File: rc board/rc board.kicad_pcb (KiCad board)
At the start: 2 copper layers, 12 parts, among them U1 DRV10983

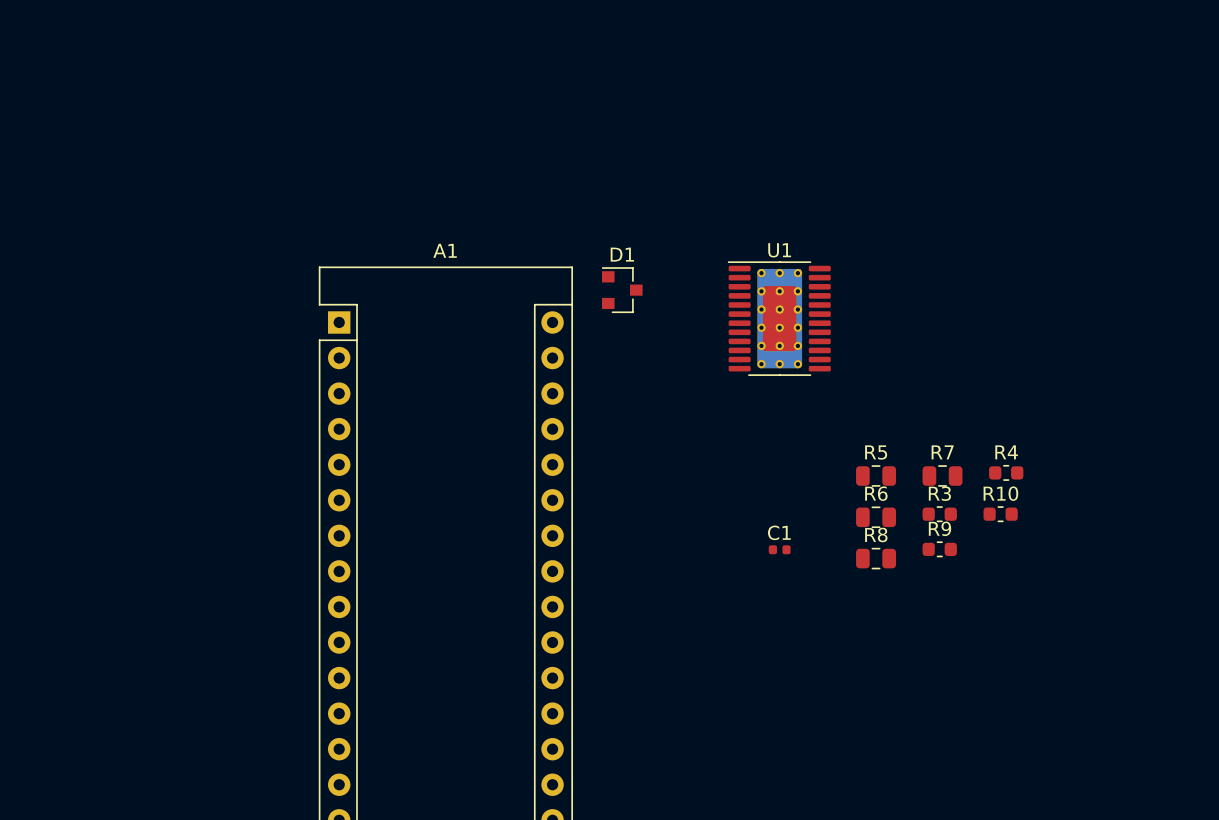
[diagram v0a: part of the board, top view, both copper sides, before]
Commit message: Finiched the driver part, and assigned the IOs to the uC.
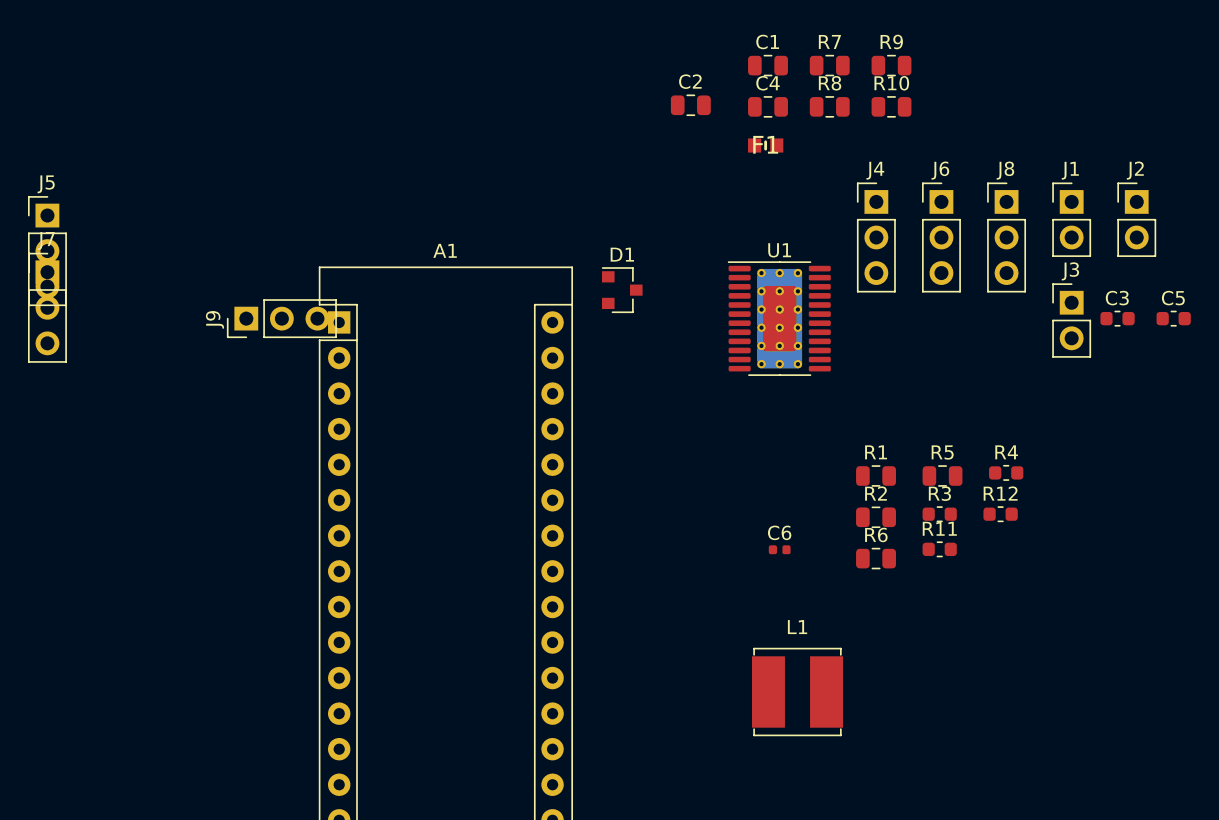
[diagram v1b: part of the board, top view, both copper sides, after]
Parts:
- added C1: 10uF, Capacitor_SMD:C_0805_2012Metric, F.Cu at (104.6, 11.1)
- added C2: 10uF, Capacitor_SMD:C_0805_2012Metric, F.Cu at (99.1, 14.0)
- added C3: 0.1uF, Capacitor_SMD:C_0603_1608Metric, F.Cu at (129.5, 29.2)
- added C4: 10uF, Capacitor_SMD:C_0805_2012Metric, F.Cu at (104.6, 14.1)
- added C5: 1uF, Capacitor_SMD:C_0603_1608Metric, F.Cu at (133.6, 29.2)
- added F1: 370mA, Fuse:FUSC1607X85N, F.Cu at (104.4, 16.8)
- added J1: Throttle_bypass, Connector_PinHeader_2.54mm:PinHeader_1x02_P2.54mm_Vertical, F.Cu at (126.3, 20.9)
- added J2: CH3_bypass, Connector_PinHeader_2.54mm:PinHeader_1x02_P2.54mm_Vertical, F.Cu at (130.9, 20.9)
- added J3: Steering_bypass, Connector_PinHeader_2.54mm:PinHeader_1x02_P2.54mm_Vertical, F.Cu at (126.3, 28.1)
- added J4: Throttle_in, Connector_PinHeader_2.54mm:PinHeader_1x03_P2.54mm_Vertical, F.Cu at (112.3, 20.9)
- added J5: Throttle_out, Connector_PinHeader_2.54mm:PinHeader_1x03_P2.54mm_Vertical, F.Cu at (53.1, 21.8)
- added J6: CH3_in, Connector_PinHeader_2.54mm:PinHeader_1x03_P2.54mm_Vertical, F.Cu at (117.0, 20.9)
- added J7: CH3_out, Connector_PinHeader_2.54mm:PinHeader_1x03_P2.54mm_Vertical, F.Cu at (53.1, 25.9)
- added J8: Steering_in, Connector_PinHeader_2.54mm:PinHeader_1x03_P2.54mm_Vertical, F.Cu at (121.6, 20.9)
- added J9: Steering_out, Connector_PinHeader_2.54mm:PinHeader_1x03_P2.54mm_Vertical, F.Cu at (67.3, 29.2)
- added L1: L_Core_Ferrite_Small, Inductor_SMD:L_Bourns_SRN6045TA, F.Cu at (106.7, 55.9)
- added R10: 10, Resistor_SMD:R_0805_2012Metric, F.Cu at (113.4, 14.1)
- added R7: 10, Resistor_SMD:R_0805_2012Metric, F.Cu at (109.0, 11.1)
- added R8: 10, Resistor_SMD:R_0805_2012Metric, F.Cu at (109.0, 14.1)
- added R9: 10, Resistor_SMD:R_0805_2012Metric, F.Cu at (113.4, 11.1)
- renumbered C1 to C6, R5 to R1, R9 to R11, R10 to R12, R6 to R2, R7 to R5, R8 to R6
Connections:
- C6 pad 1: Net-(C1-Pad1) -> Net-(C6-Pad1)
- C6 pad 2: Net-(C1-Pad2) -> Net-(C6-Pad2)
- U1 pad 1: (no net) -> Net-(C3-Pad2)
- U1 pad 17: Net-(U1-Pad17) -> U_0
- U1 pad 18: Net-(U1-Pad18) -> U_0
- U1 pad 19: Net-(U1-Pad19) -> V_0
- U1 pad 2: Net-(U1-Pad2) -> Net-(C6-Pad1)
- U1 pad 20: Net-(U1-Pad20) -> V_0
- U1 pad 21: Net-(U1-Pad21) -> W_0
- U1 pad 22: Net-(U1-Pad22) -> W_0
- U1 pad 3: Net-(U1-Pad3) -> Net-(C6-Pad2)
- U1 pad 6: Net-(U1-Pad6) -> +5V_0

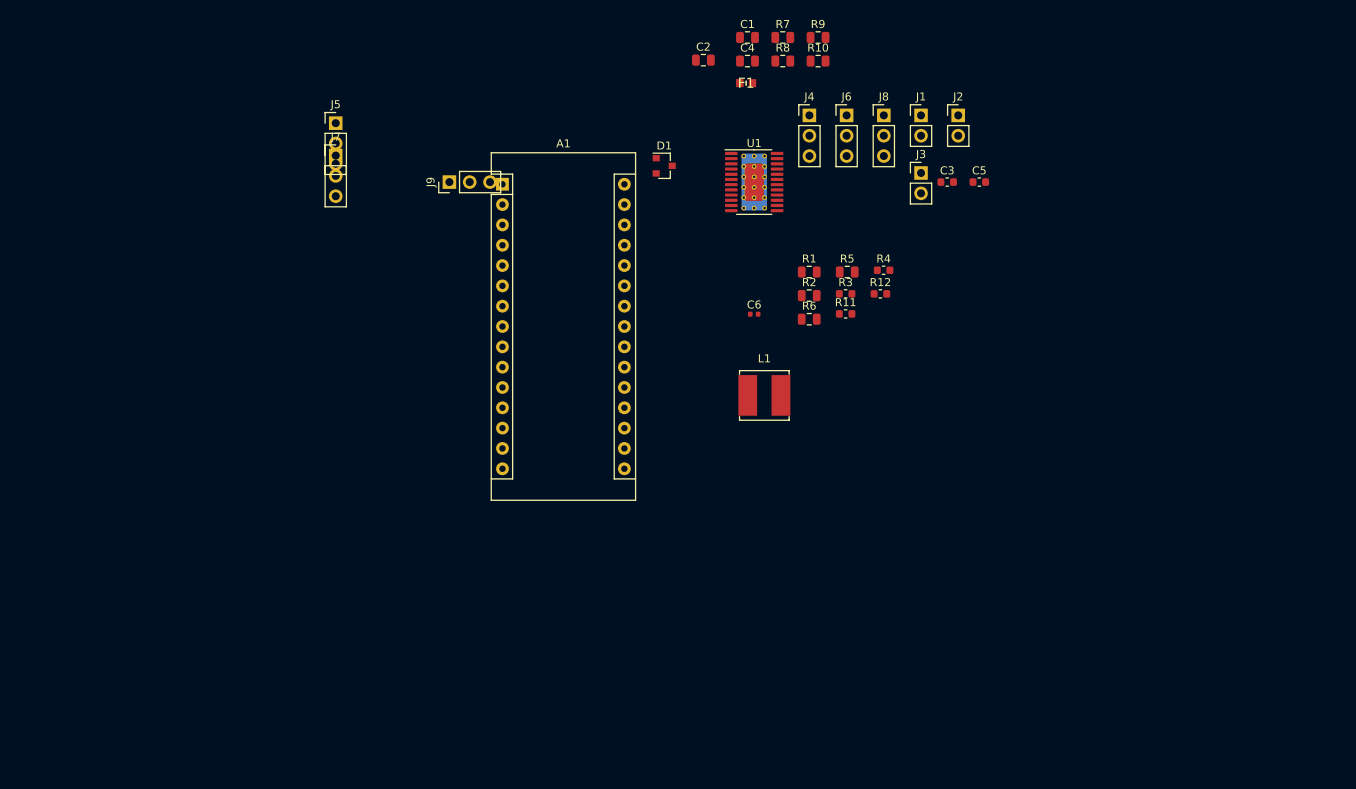
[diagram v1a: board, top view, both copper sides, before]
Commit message: Added schottkyes for automatic battery compatibility, and started component layout.
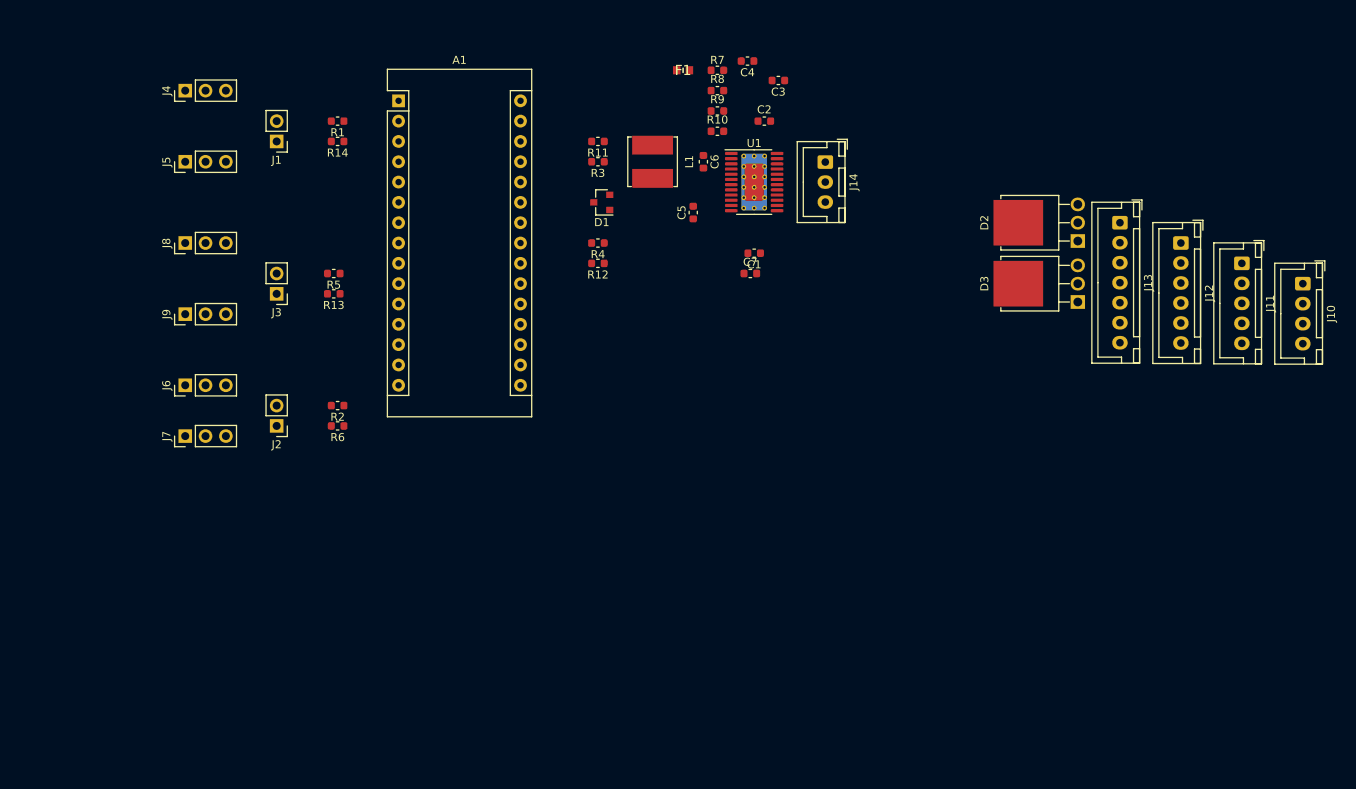
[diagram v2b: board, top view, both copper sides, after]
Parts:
- added C7: 10uF, Capacitor_SMD:C_0603_1608Metric, F.Cu at (104.9, 40.6)
- added D2: MBR2045CTI, Package_TO_SOT_THT:TO-251-3-1EP_Horizontal_TabDown, F.Cu at (145.9, 36.6)
- added D3: MBR2045CTI, Package_TO_SOT_THT:TO-251-3-1EP_Horizontal_TabDown, F.Cu at (145.9, 44.2)
- added J10: 3S, Connector_JST:JST_XH_B4B-XH-A_1x04_P2.50mm_Vertical, F.Cu at (174.0, 41.9)
- added J11: 4S, Connector_JST:JST_XH_B5B-XH-A_1x05_P2.50mm_Vertical, F.Cu at (166.4, 39.4)
- added J12: 5S, Connector_JST:JST_XH_B6B-XH-A_1x06_P2.50mm_Vertical, F.Cu at (158.8, 36.8)
- added J13: 6S, Connector_JST:JST_XH_B7B-XH-A_1x07_P2.50mm_Vertical, F.Cu at (151.1, 34.3)
- added J14: Mot_0, Connector_JST:JST_XH_B3B-XH-A_1x03_P2.50mm_Vertical, F.Cu at (114.3, 26.7)
- added R13: 10k, Resistor_SMD:R_0603_1608Metric, F.Cu at (52.9, 43.2)
- added R14: 10k, Resistor_SMD:R_0603_1608Metric, F.Cu at (53.3, 24.1)
- C1: value 10uF -> 1uF; footprint Capacitor_SMD:C_0805_2012Metric -> Capacitor_SMD:C_0603_1608Metric
- C2, C4: footprint Capacitor_SMD:C_0805_2012Metric -> Capacitor_SMD:C_0603_1608Metric
- C3: value 0.1uF -> 100nF
- C6: value 0.01nF -> 10nF; footprint Capacitor_SMD:C_0402_1005Metric -> Capacitor_SMD:C_0603_1608Metric
- J1: value Throttle_bypass -> Bypass
- J2: value CH3_bypass -> Bypass
- J3: value Steering_bypass -> Bypass
- L1: value L_Core_Ferrite_Small -> 47 uH
- R1, R2, R5, R6: value 10 -> 10k; footprint Resistor_SMD:R_0805_2012Metric -> Resistor_SMD:R_0603_1608Metric
- R10, R7, R8, R9: footprint Resistor_SMD:R_0805_2012Metric -> Resistor_SMD:R_0603_1608Metric
- moved J2 93.6 mm to (45.7, 59.7), turned to 180 degrees
- moved J6 89.3 mm to (34.3, 54.6), turned to 90 degrees
- moved J8 88.8 mm to (34.3, 36.8), turned to 90 degrees
- moved J3 81.9 mm to (45.7, 43.2), turned to 180 degrees
- moved J1 80.6 mm to (45.7, 24.1), turned to 180 degrees
- moved J4 78.1 mm to (34.3, 17.8), turned to 90 degrees
- moved R5 64.2 mm to (52.9, 40.6), turned to 180 degrees
- moved R1 61.9 mm to (53.3, 21.6), turned to 180 degrees
- moved R2 60.5 mm to (53.3, 57.1), turned to 180 degrees
- moved R6 60.4 mm to (53.3, 59.7), turned to 180 degrees
- moved J7 39.8 mm to (34.3, 61.0), turned to 90 degrees
- moved R11 37.7 mm to (85.9, 24.1), turned to 180 degrees
- moved J9 36.9 mm to (34.3, 45.7)
- moved C5 36.0 mm to (97.8, 33.0), turned to 90 degrees
- moved R4 35.9 mm to (85.9, 36.8), turned to 180 degrees
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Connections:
- net Net-(A1-Pad10) renamed EN_3
- net Net-(A1-Pad7) renamed EN_1
- net Net-(A1-Pad9) renamed EN_2
- net Net-(J1-Pad1) renamed Throttle_in
- net Net-(J3-Pad1) renamed Steering_in
- A1 pad 11: Net-(A1-Pad11) -> DIR
- A1 pad 19: Net-(A1-Pad19) -> Batt_0
- A1 pad 20: Net-(A1-Pad20) -> Batt_1
- A1 pad 21: Net-(A1-Pad21) -> Batt_2
- A1 pad 22: Net-(A1-Pad22) -> Batt_3
- A1 pad 25: Net-(A1-Pad25) -> Batt_4
- A1 pad 26: Net-(A1-Pad26) -> Batt_5
- A1 pad 27: +3V3 -> +5V
- A1 pad 5: Net-(A1-Pad5) -> EN_0
- C1 pad 2: +3V3 -> Net-(C1-Pad2)
- J1 pad 2: Net-(J1-Pad2) -> Throttle_out
- J2 pad 1: Net-(J2-Pad1) -> CH3_in
- J2 pad 2: Net-(J2-Pad2) -> CH3_out
- J3 pad 2: Net-(J3-Pad2) -> Steering_out
- J4 pad 3: Net-(J1-Pad2) -> Throttle_out
- J6 pad 3: Net-(J2-Pad2) -> CH3_out
- J7 pad 3: Net-(J2-Pad1) -> CH3_in
- J8 pad 3: Net-(J3-Pad2) -> Steering_out
- R1 pad 1: +3V3 -> Net-(A1-Pad6)
- R1 pad 2: +3.3V_0 -> Throttle_out
- R2 pad 1: +3V3 -> Net-(A1-Pad8)
- R2 pad 2: +3.3V_1 -> CH3_out
- R3 pad 1: Net-(D1-Pad1) -> Net-(D1-Pad2)
- R4 pad 1: Net-(D1-Pad2) -> Net-(D1-Pad1)
- R5 pad 1: +3V3 -> Net-(A1-Pad12)
- R5 pad 2: +3.3V_2 -> Steering_out
- R6 pad 1: +3V3 -> Net-(A1-Pad13)
- R6 pad 2: +3.3V_3 -> CH3_in
- U1 pad 10: Net-(D1-Pad1) -> Net-(D1-Pad2)
- U1 pad 11: Net-(D1-Pad2) -> Net-(D1-Pad1)
- U1 pad 14: DIR_0 -> DIR
- U1 pad 9: +3.3V_0 -> Net-(C1-Pad2)

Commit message: More routing, added the second driver.
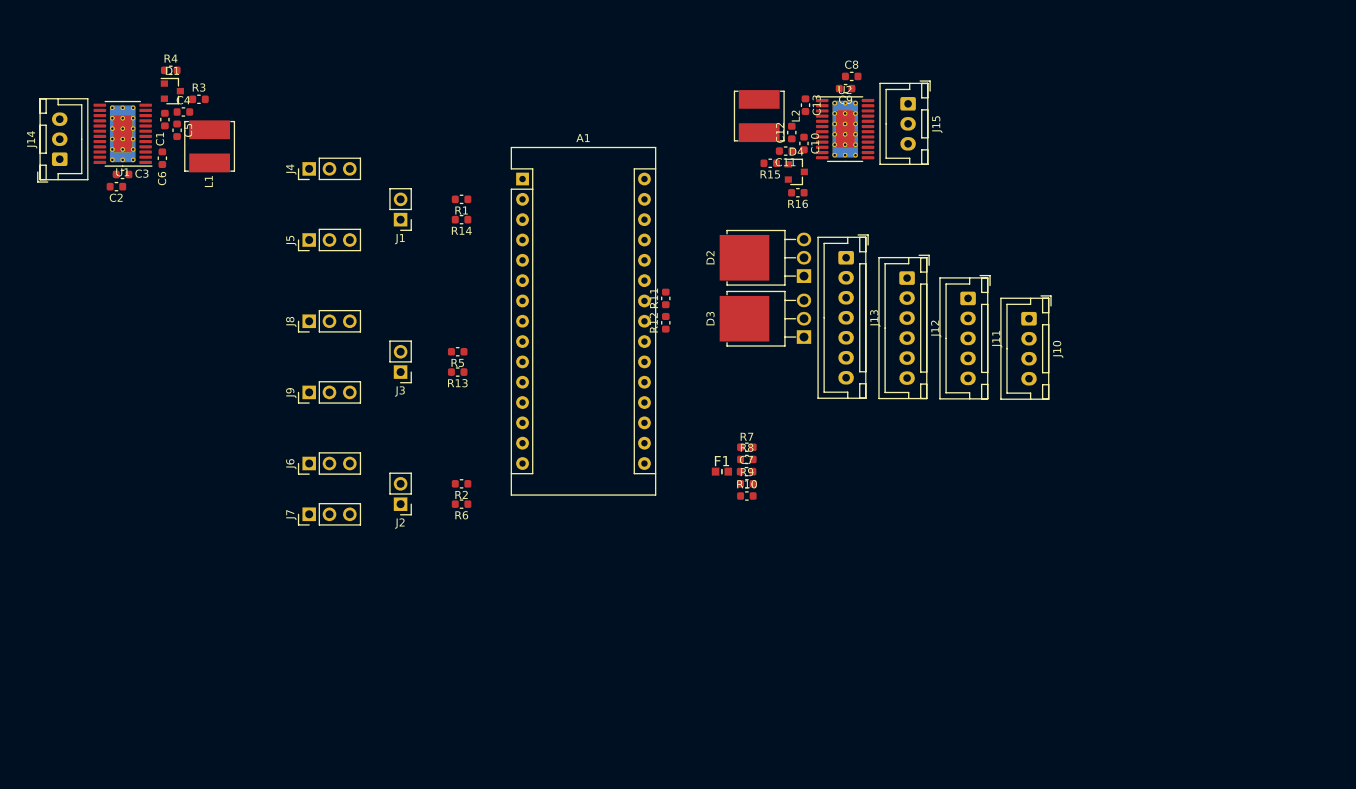
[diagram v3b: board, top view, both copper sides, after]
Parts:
- added C10: 1uF, Capacitor_SMD:C_0603_1608Metric, F.Cu at (111.6, 24.4)
- added C11: 10uF, Capacitor_SMD:C_0603_1608Metric, F.Cu at (109.3, 25.3)
- added C12: 1uF, Capacitor_SMD:C_0603_1608Metric, F.Cu at (110.1, 23.0)
- added C13: 10nF, Capacitor_SMD:C_0603_1608Metric, F.Cu at (111.8, 19.6)
- added C8: 10uF, Capacitor_SMD:C_0603_1608Metric, F.Cu at (117.6, 16.0)
- added C9: 100nF, Capacitor_SMD:C_0603_1608Metric, F.Cu at (116.8, 17.5)
- added D4: BAW56LT3G, Package_TO_SOT_SMD:SOT-23, F.Cu at (110.7, 27.9)
- added J15: Mot_0, Connector_JST:JST_XH_B3B-XH-A_1x03_P2.50mm_Vertical, F.Cu at (124.7, 19.4)
- added L2: 47 uH, Inductor_SMD:L_Bourns_SRN6045TA, F.Cu at (106.0, 21.0)
- added R15: 10k, Resistor_SMD:R_0603_1608Metric, F.Cu at (107.4, 26.9)
- added R16: 10k, Resistor_SMD:R_0603_1608Metric, F.Cu at (110.9, 30.5)
- added U2: DRV10983, Package_SO:HTSSOP-24-1EP_4.4x7.8mm_P0.65mm_EP3.4x7.8mm_Mask2.4x4.68mm_ThermalVias, F.Cu at (116.8, 22.6)
- moved J14 95.7 mm to (18.6, 26.4), turned to 90 degrees
- moved C3 82.8 mm to (26.5, 28.3), turned to 0 degrees
- moved C2 81.4 mm to (25.7, 29.8), turned to 180 degrees
- moved U1 79.2 mm to (26.5, 23.2), turned to 180 degrees
- moved C1 75.5 mm to (31.8, 21.4), turned to 90 degrees
- moved C4 70.8 mm to (34.1, 20.4), turned to 0 degrees
- moved C6 67.6 mm to (31.4, 26.2), turned to 90 degrees
- moved C5 65.3 mm to (33.3, 22.7), turned to 270 degrees
- moved R4 57.6 mm to (32.5, 15.2), turned to 0 degrees
- moved D1 55.4 mm to (32.7, 17.8), turned to 0 degrees
- moved L1 55.4 mm to (37.3, 24.7), turned to 90 degrees
- moved R3 50.5 mm to (36.0, 18.9), turned to 0 degrees
- moved F1 50.4 mm to (101.4, 65.4)
- moved R7 47.3 mm to (104.5, 62.4)
- moved R9 46.8 mm to (104.5, 66.9)
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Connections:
- A1 pad 17: Net-(A1-Pad17) -> +3V3
- A1 pad 19: Batt_0 -> Batt_0_sense
- A1 pad 20: Batt_1 -> Batt_1_sense
- A1 pad 21: Batt_2 -> Batt_2_sense
- A1 pad 22: Batt_3 -> Batt_3_sense
- A1 pad 25: Batt_4 -> Batt_4_sense
- A1 pad 26: Batt_5 -> Batt_5_sense
- U1 pad 25: (no net) -> GND
